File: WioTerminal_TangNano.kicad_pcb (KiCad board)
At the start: 2 copper layers, 68 x 52.5 mm, 35 parts, among them J1 Raspberry_Pi_2_3, J2 TangNano_Left, J3 GROVE, J4 GROVE, J5 TangNano_JTAG_L, J6 TangNano_Right, J7 TangNano_JTAG_R, J8 HDMI_A, J9 Raspberry_Pi_2_3, U3 ATECC608A

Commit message: Routing finished
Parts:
- removed C10: 100n, Capacitor_SMD:C_0603_1608Metric
- removed U3: ATECC608A, Package_DFN_QFN:DFN-8-1EP_3x2mm_P0.5mm_EP1.3x1.5mm
- C12, C13, R11, R12, R3, R4: moved to B.Cu
- moved LOGO1 27.6 mm to (41.6, -11.3)
- moved R17 16.1 mm to (42.3, -7.65)
- moved C13 7.82 mm to (6.20, -19.1)
- moved C12 7.32 mm to (6.10, -31.8)
- moved R14 3.46 mm to (16.8, -35.1)
- moved R13 2.58 mm to (16.8, -33.6)
- moved R12 1.37 mm to (42.1, -34.0)
- moved R2 0.50 mm to (49.2, -32.2), turned to 90 degrees
- moved R4 0.49 mm to (44.1, -19.5)
- moved R1 0.41 mm to (54.2, -32.3)
- moved R3 0.41 mm to (46.6, -19.5)
- moved R11 0.32 mm to (42.1, -35.5)
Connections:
- J6 pad 16: /VBANK0_3 -> +3V3
- J6 pad 17: /VBANK0_3 -> +3V3
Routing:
- net +5V: track 0.00 -> 113.4 mm, vias 0 -> 3
- net +3V3: track 0.00 -> 106.4 mm, vias 0 -> 6
- net /RXD: track 0.00 -> 73.3 mm, vias 0 -> 4
- net /TXD: track 0.00 -> 70.7 mm, vias 0 -> 4
- net GND: track 0.00 -> 56.6 mm, vias 0 -> 17
- net /SDA: track 0.00 -> 40.0 mm, vias 0 -> 2
- net /TCK: track 0.00 -> 37.4 mm, vias 0 -> 1
- net /SCL: track 0.00 -> 34.0 mm, vias 0 -> 2
- net /TDO: track 0.00 -> 28.2 mm, vias 0 -> 1
- net /TMS: track 0.00 -> 27.9 mm, vias 0 -> 1
- net /TDI: track 0.00 -> 24.1 mm, vias 0 -> 1
- net /IOB11B: track 0.00 -> 21.3 mm, vias 0 -> 1
- net /I2C1_SDA: track 0.00 -> 19.6 mm, vias 0 -> 1
- net /I2C1_SCL: track 0.00 -> 18.0 mm, vias 0 -> 2
- net /I2C0_SCL: track 0.00 -> 16.0 mm, vias 0 -> 1
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- added copper zone on F.Cu, net GND
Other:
- board text added: "Tang Nano Adapter for Wio Terminal 2020-06-15 Rev.A by Kenta IDA (@ciniml)"
- board text removed: "AA/AAA Battery Chassis for Wio Terminal 2020-05-28 Rev.A by Kenta IDA (@ciniml)"

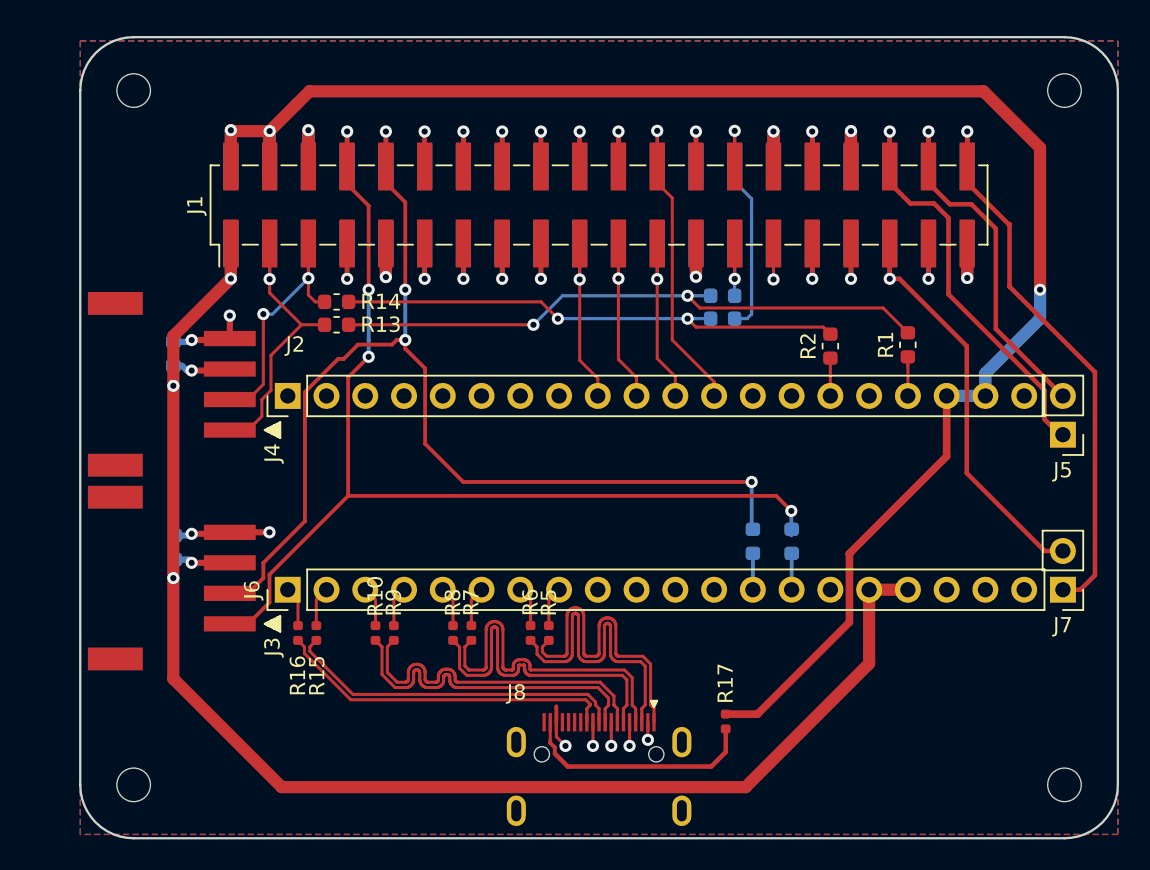
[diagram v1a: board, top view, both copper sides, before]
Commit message: Fix that TangNano board width was wrong.
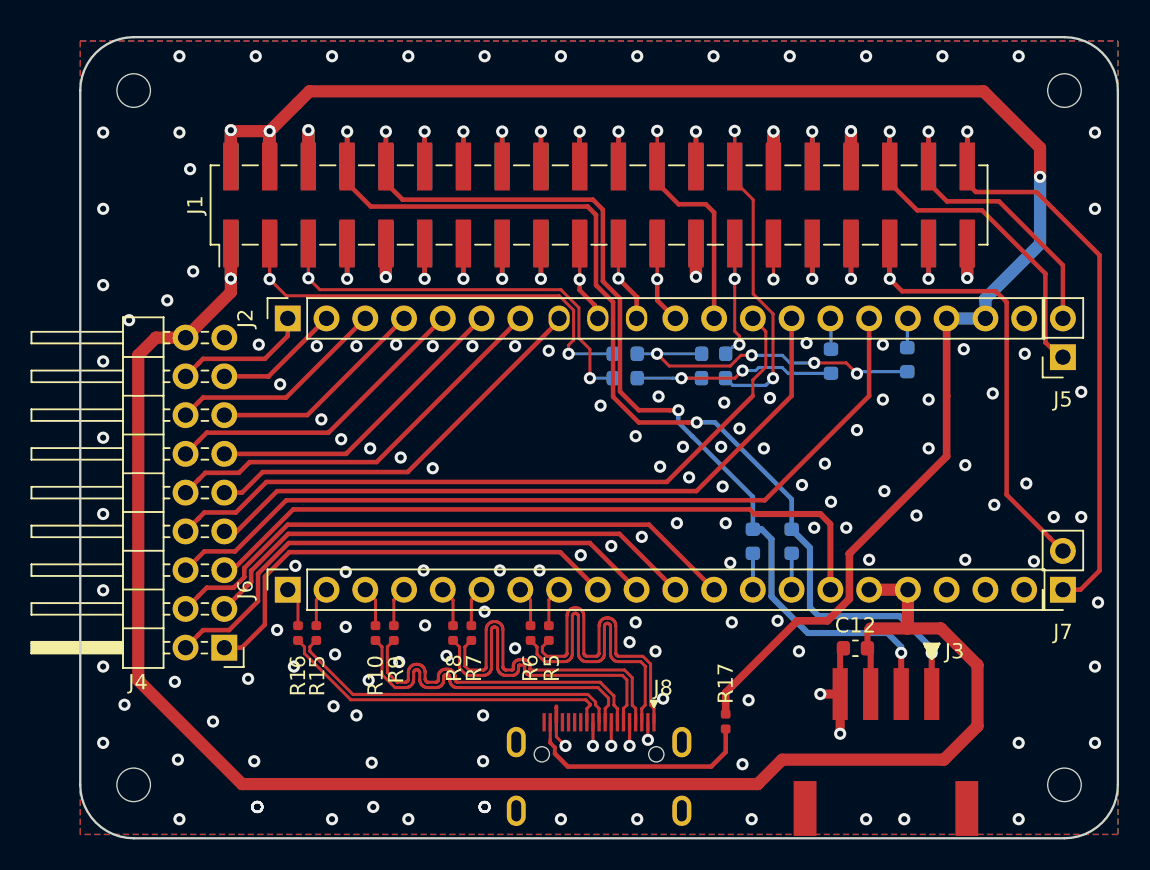
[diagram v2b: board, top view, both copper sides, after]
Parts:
- removed C13: 1u, Capacitor_SMD:C_0603_1608Metric
- C12: moved to F.Cu
- J2, J6: footprint Connector_PinHeader_2.54mm:PinHeader_1x20_P2.54mm_Vertical -> Connector_PinSocket_2.54mm:PinSocket_1x20_P2.54mm_Vertical
- J4: value GROVE -> Conn_01x18; footprint local:PHS-4AW -> Connector_PinHeader_2.54mm:PinHeader_2x09_P2.54mm_Horizontal
- J5, J7: footprint Connector_PinHeader_2.54mm:PinHeader_1x02_P2.54mm_Vertical -> Connector_PinSocket_2.54mm:PinSocket_1x02_P2.54mm_Vertical
- R1, R13, R14, R2: moved to B.Cu
- moved C12 48.7 mm to (50.8, -12.4), turned to 180 degrees
- moved J3 45.7 mm to (52.8, -7.75), turned to 0 degrees
- moved R14 19.6 mm to (35.7, -30.1)
- moved R13 19.0 mm to (35.7, -31.8)
- moved J4 17.3 mm to (9.44, -12.5), turned to 180 degrees
- moved J2 5.08 mm to (13.6, -34.1)
- moved J5 5.08 mm to (64.4, -31.5)
- moved R12 3.95 mm to (41.5, -30.1)
- moved R11 3.85 mm to (41.5, -31.8)
- moved R2 0.99 mm to (49.2, -31.3), turned to 270 degrees
- moved R1 0.98 mm to (54.2, -31.4), turned to 270 degrees
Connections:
- J2 pad 1: (no net) -> /R0
- J2 pad 13: (no net) -> /IOB14A
- J2 pad 14: (no net) -> /IOB14B
- J2 pad 16: (no net) -> /IOV11A
- J2 pad 2: (no net) -> /R1
- J2 pad 3: (no net) -> /R2
- J2 pad 4: (no net) -> /R3
- J2 pad 5: (no net) -> /R4
- J2 pad 6: (no net) -> /G0
- J2 pad 7: (no net) -> /G1
- J2 pad 8: (no net) -> /G2
- J4 pad 1: /I2C1_SDA -> /LCD_CLK
- J4 pad 2: /I2C1_SCL -> /LCD_HSYNC
- J4 pad 3: +3V3 -> /LCD_VSYNC
- J4 pad 4: GND -> /LCD_DE
- J6 pad 10: (no net) -> /LCD_HSYNC
- J6 pad 11: (no net) -> /LCD_VSYNC
- J6 pad 12: (no net) -> /LCD_DE
- J6 pad 15: (no net) -> /IOB3A
- J6 pad 9: (no net) -> /LCD_CLK
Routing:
- net /IOV11A: track 0.00 -> 54.6 mm
- net /IOB14A: track 0.00 -> 46.6 mm
- net /IOB3A: track 0.00 -> 46.1 mm
- net /IOB14B: track 0.00 -> 45.9 mm
- net /LCD_DE: track 0.00 -> 39.0 mm
- net /LCD_HSYNC: track 0.00 -> 34.7 mm
- net /LCD_VSYNC: track 0.00 -> 33.5 mm
- net /LCD_CLK: track 0.00 -> 29.9 mm
- net /G2: track 0.00 -> 26.8 mm
- net /G1: track 0.00 -> 26.7 mm
- net /R4: track 0.00 -> 20.5 mm
- net /G0: track 0.00 -> 20.5 mm
- net /SCL: track 34.0 -> 14.5 mm
- net /SDA: track 40.0 -> 21.8 mm, vias 2 -> 4
- net /R3: track 0.00 -> 14.4 mm
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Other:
- board text added: "14B/14A"
- board text added: "3A/11A"
- board text added: "CLK/HSYNC"
- board text added: "G0/R4"
- board text added: "G2/G1"
- board text added: "GND/+3V3"
- board text added: "R1/R0"
- board text added: "R3/R2"
- board text added: "VSYNC/DE"

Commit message: Fix that HDMI Type-C pin assignment was wrong. Add PTH to use concatenating header.
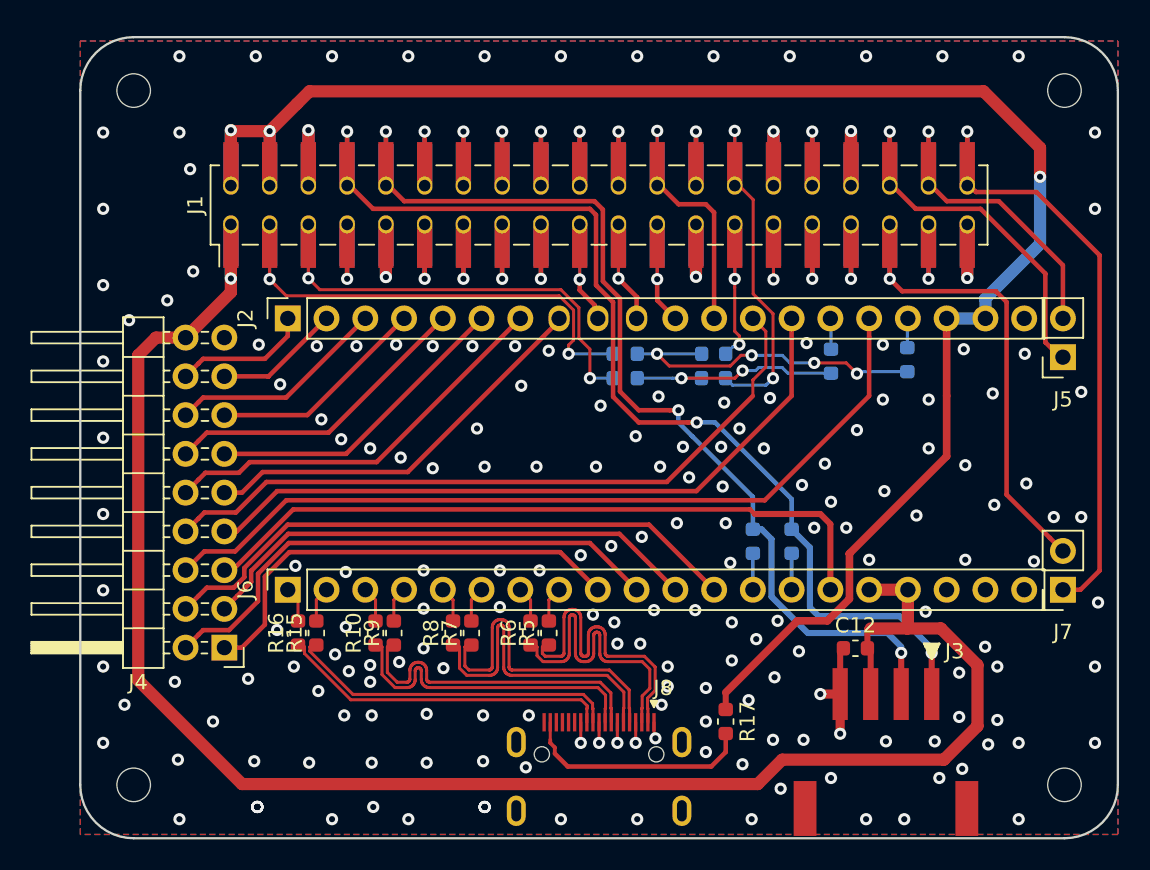
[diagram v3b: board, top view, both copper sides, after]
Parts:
- J1: footprint Connector_PinHeader_2.54mm:PinHeader_2x20_P2.54mm_Vertical_SMD -> local:PinHeader_2x20_P2.54mm_Vertical_SMD
- J8: value HDMI_A -> HDMI_C_1.3
- R10, R15, R16, R17, R5, R6, R7, R8, R9: footprint Resistor_SMD:R_0402_1005Metric -> Resistor_SMD:R_0603_1608Metric
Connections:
- J8 pad 1: /HDMI_D2_P -> GND
- J8 pad 10: /HDMI_CK_P -> GND
- J8 pad 11: GND -> /HDMI_CK_P
- J8 pad 13: (no net) -> GND
- J8 pad 17: GND -> (no net)
- J8 pad 2: GND -> /HDMI_D2_P
- J8 pad 4: /HDMI_D1_P -> GND
- J8 pad 5: GND -> /HDMI_D1_P
- J8 pad 7: /HDMI_D0_P -> GND
- J8 pad 8: GND -> /HDMI_D0_P
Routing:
- net GND: track 52.1 -> 49.9 mm, vias 156 -> 195
- net /HDMI_D1_P: track 22.8 -> 21.4 mm
- net /HDMI_D1_N: track 22.8 -> 21.4 mm
- net /HDMI_D0_P: track 22.5 -> 21.4 mm
- net /HDMI_D0_N: track 22.5 -> 21.4 mm
- net /HDMI_D2_P: track 22.4 -> 21.4 mm
- net /HDMI_D2_N: track 22.4 -> 21.4 mm
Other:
- board text added: "Tang Nano Adapter for Wio Terminal 2020-07-13 Rev.B by Kenta IDA (@ciniml)"
- board text removed: "Tang Nano Adapter for Wio Terminal 2020-06-15 Rev.A by Kenta IDA (@ciniml)"
